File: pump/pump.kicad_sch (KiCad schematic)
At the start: 10 parts

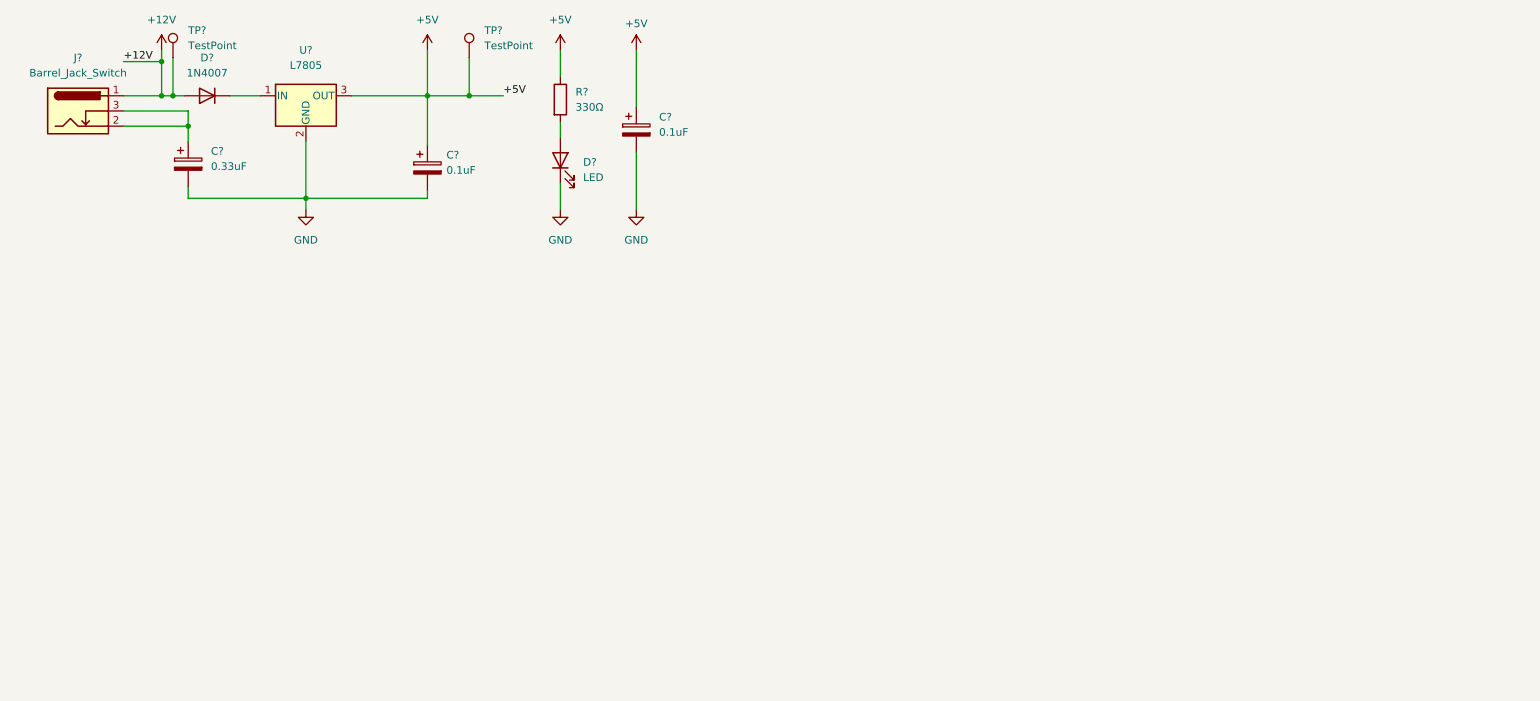
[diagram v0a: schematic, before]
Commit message: Version 2022.09.20 - Added Terminal Blocks
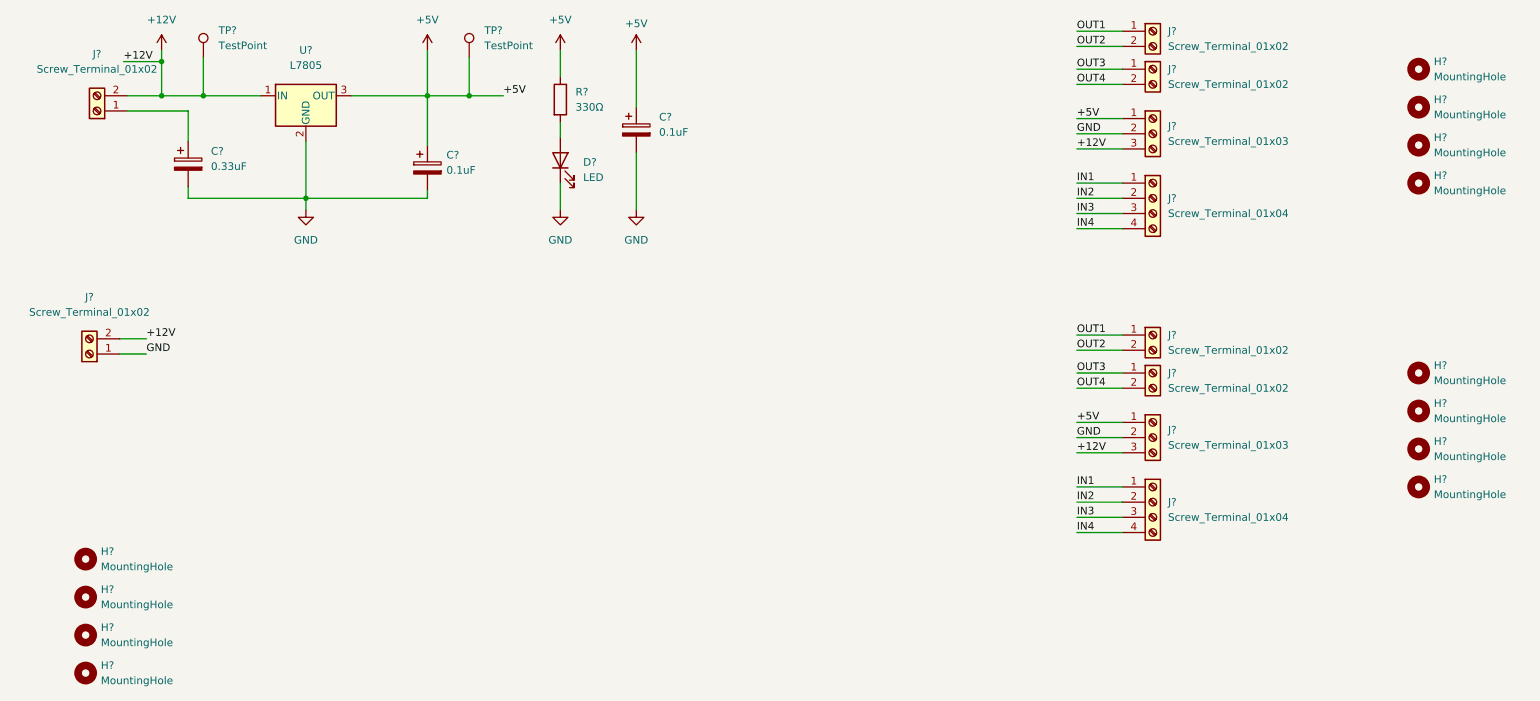
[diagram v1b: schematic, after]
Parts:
- removed D?: 1N4007, Diode_THT:D_DO-41_SOD81_P10.16mm_Horizontal, symbol Diode:1N4007
- removed J?: Barrel_Jack_Switch, Connector_BarrelJack:BarrelJack_Horizontal, symbol Connector:Barrel_Jack_Switch
- added H? (x11): MountingHole, MountingHole:MountingHole_3.2mm_M3, symbol Mechanical:MountingHole
- added H?: MountingHole, symbol Mechanical:MountingHole
- added J? (x2): Screw_Terminal_01x03, symbol Connector:Screw_Terminal_01x03
- added J? (x6): Screw_Terminal_01x02, symbol Connector:Screw_Terminal_01x02
- added J? (x2): Screw_Terminal_01x04, symbol Connector:Screw_Terminal_01x04
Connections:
- net +12V: now also U?.1 (IN), J?.2 (Pin_2), J?.2 (Pin_2), J?.3 (Pin_3), J?.3 (Pin_3)
- net +5V: now also J?.1 (Pin_1), J?.1 (Pin_1)
- net GND: now also J?.1 (Pin_1), J?.2 (Pin_2), J?.2 (Pin_2)
- net at C?.1: now also J?.1 (Pin_1)
- new net IN1: J?.1 (Pin_1), J?.1 (Pin_1)
- new net IN2: J?.2 (Pin_2), J?.2 (Pin_2)
- new net IN3: J?.3 (Pin_3), J?.3 (Pin_3)
- new net IN4: J?.4 (Pin_4), J?.4 (Pin_4)
- new net OUT1: J?.1 (Pin_1), J?.1 (Pin_1)
- new net OUT2: J?.2 (Pin_2), J?.2 (Pin_2)
- new net OUT3: J?.1 (Pin_1), J?.1 (Pin_1)
- new net OUT4: J?.2 (Pin_2), J?.2 (Pin_2)
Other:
- moved on the sheet: TP?
